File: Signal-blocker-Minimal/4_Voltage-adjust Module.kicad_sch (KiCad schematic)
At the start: 9 parts, among them U4 AMS1117A-ADJ

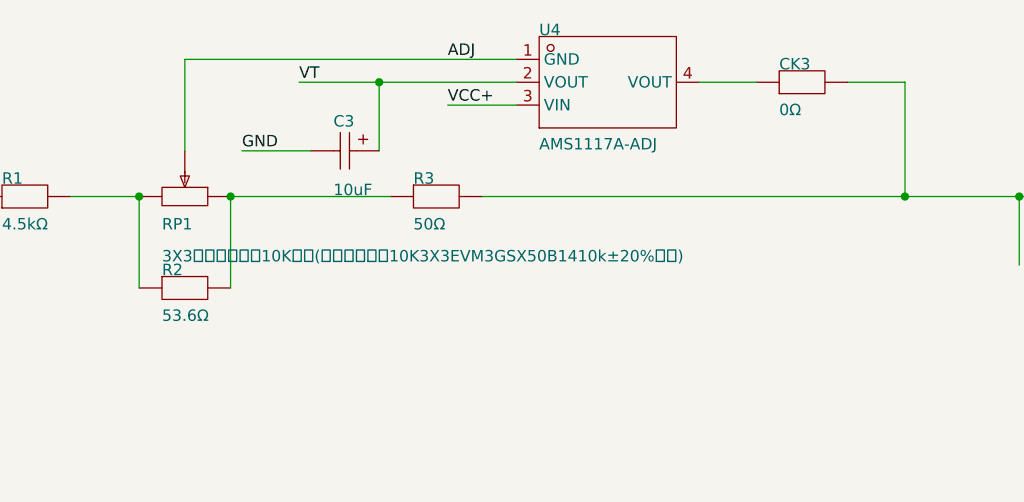
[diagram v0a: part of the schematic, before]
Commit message: Version 2.1 Update！
Fix some circuit!
More stabler!
Replace all the restrictor and capacitor into 0603 packaging!
create BOM excel,Bill of Material.
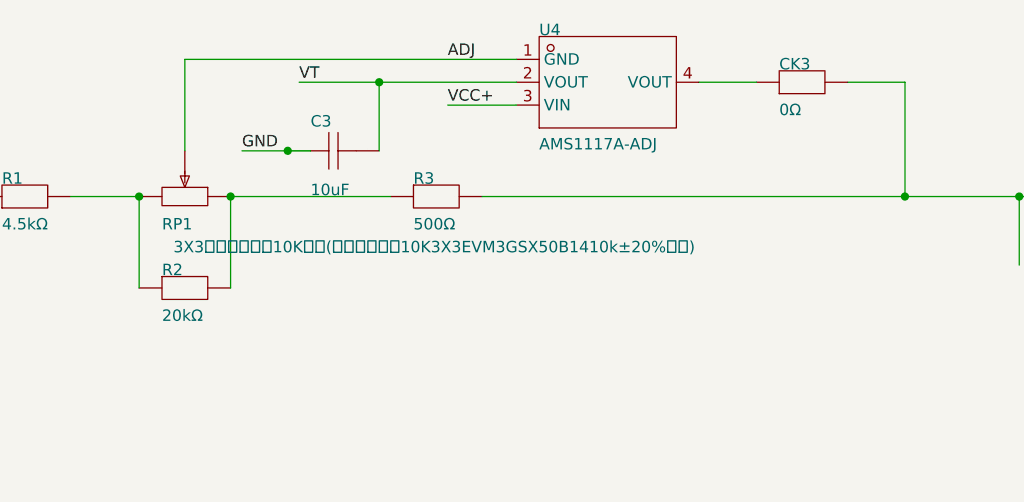
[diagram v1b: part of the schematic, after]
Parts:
- removed ?: (no value), ProPrj_Sig-easyedapro:, symbol ProPrj_Sig-easyedapro:Drawing-Symbol_A4
- removed C3: 10uF, ProPrj_Sig-easyedapro:CAP-SMD_L3.2-W1.6-RD-C7171, symbol ProPrj_Sig-easyedapro:TAJA106K016RNJ
- removed CK2, CK3: 0Ω, ProPrj_Sig-easyedapro:R0603, symbol ProPrj_Sig-easyedapro:0Ω
- removed R1: 4.5kΩ, ProPrj_Sig-easyedapro:R0805, symbol ProPrj_Sig-easyedapro:Y16294K50000B9W
- removed R2: 53.6Ω, ProPrj_Sig-easyedapro:R0805, symbol ProPrj_Sig-easyedapro:RT0805BRD0753R6L
- removed R3: 50Ω, ProPrj_Sig-easyedapro:R0805, symbol ProPrj_Sig-easyedapro:AR05ATB0500
- removed RP1: 3X3贴片可调电阻10K可调(贴片可调电阻10K3X3EVM3GSX50B1410k±20%松下), ProPrj_Sig-easyedapro:RES-ADJ-SMD_3P-L3.0-W3.8-P1.75-BR, symbol ProPrj_Sig-easyedapro:3X3贴片可调电阻10K可调(贴片可调电阻10K3X3EVM3GSX50B1410K±20%松下)
- removed U4: AMS1117A-ADJ, ProPrj_Sig-easyedapro:SOT-223_L6.3-W3.5-P2.30-LS7.0-BR, symbol ProPrj_Sig-easyedapro:AMS1117A-ADJ
- added ?: (no value), Signal-blo-easyedapro:, symbol Signal-blo-easyedapro:Drawing-Symbol_A4
- added C3: 10uF, Signal-blo-easyedapro:C0603, symbol Signal-blo-easyedapro:HGC0603R5106M160NTHJ
- added CK2, CK3: 0Ω, Signal-blo-easyedapro:R0603, symbol Signal-blo-easyedapro:0Ω
- added R1: 4.5kΩ, Signal-blo-easyedapro:R0805, symbol Signal-blo-easyedapro:Y16294K50000B9W
- added R2: 20kΩ, Signal-blo-easyedapro:R0805, symbol Signal-blo-easyedapro:RT0805BRD0753R6L
- added R3: 500Ω, Signal-blo-easyedapro:R0805, symbol Signal-blo-easyedapro:AR05ATB0500
- added RP1: 3X3贴片可调电阻10K可调(贴片可调电阻10K3X3EVM3GSX50B1410k±20%松下), Signal-blo-easyedapro:RES-ADJ-SMD_3P-L3.0-W3.8-P1.75-BR, symbol Signal-blo-easyedapro:3X3贴片可调电阻10K可调(贴片可调电阻10K3X3EVM3GSX50B1410K±20%松下)
- added U4: AMS1117A-ADJ, Signal-blo-easyedapro:SOT-223_L6.3-W3.5-P2.30-LS7.0-BR, symbol Signal-blo-easyedapro:AMS1117A-ADJ
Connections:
- net ADJ: now also RP1.2, U4.1 (GND)
- net GND: now also C3.1
- net VCC+: now also U4.3 (VIN)
- net VCC-: now also CK3.2, R3.2
- net VCC9V+: now also CK2.1
- net VT: now also C3.2, U4.2 (VOUT)
- new net: R1.2, R2.1, RP1.1
- new net: R2.2, R3.1, RP1.3
- new net: CK3.1, U4.4 (VOUT)
- new net: CK2.2, R1.1
